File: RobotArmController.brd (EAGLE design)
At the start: 83.6 x 34.8 mm, 67 parts, among them M1 M02LOCK, M2 M02LOCK, M3 M02LOCK, M4 M02LOCK, M5 M02LOCK

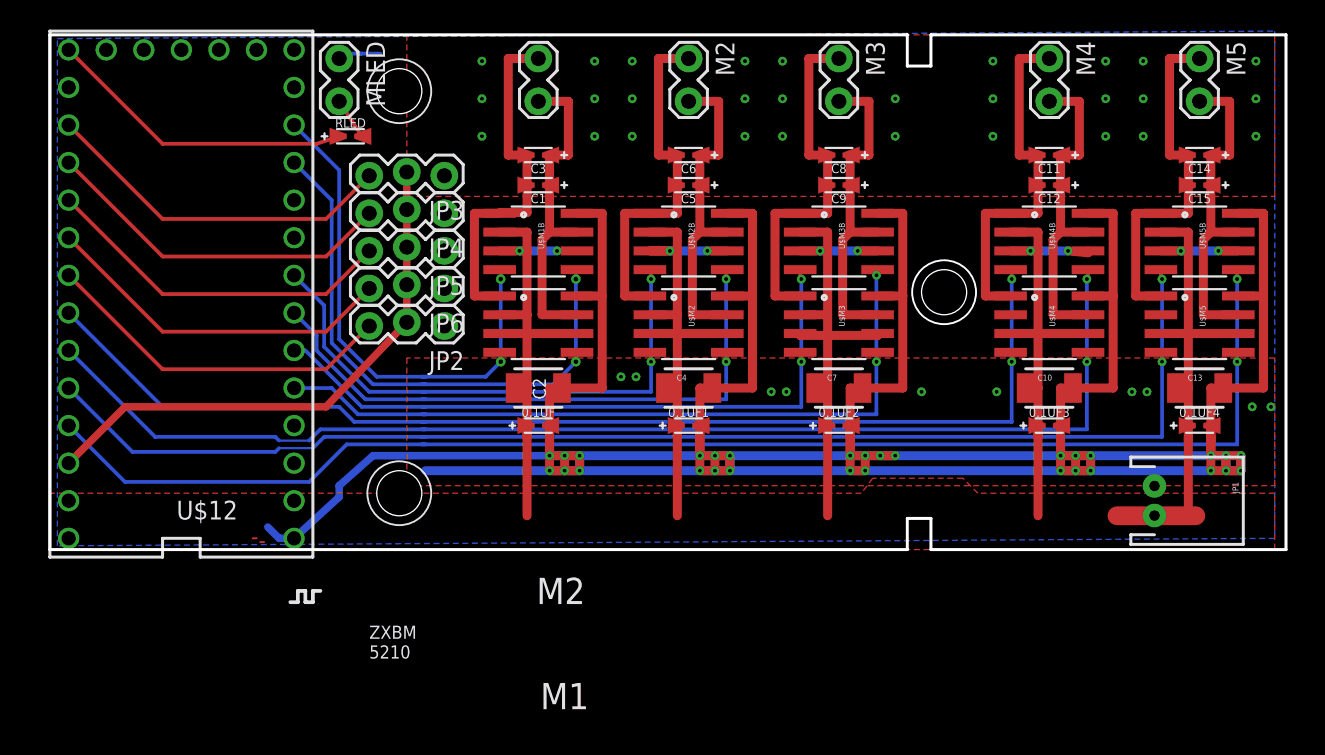
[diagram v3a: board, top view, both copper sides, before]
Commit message: Adjust for silkscreen and labels
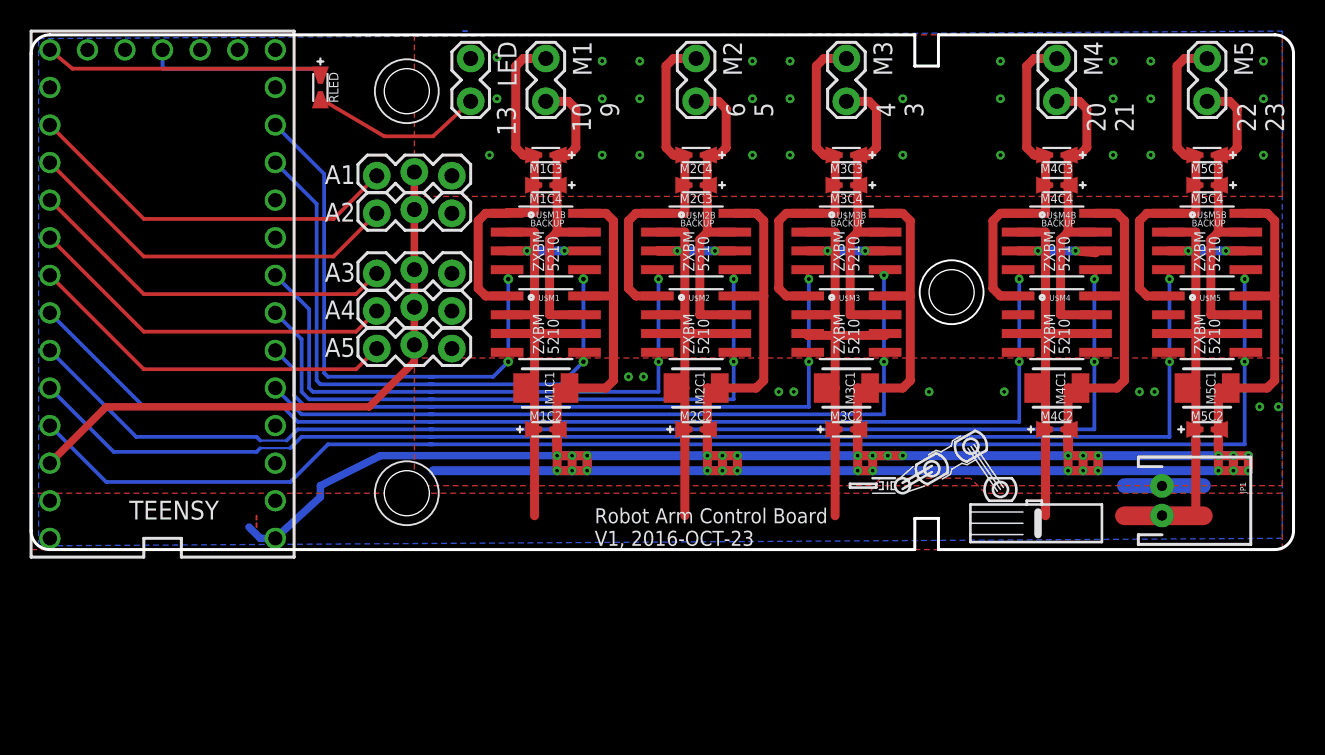
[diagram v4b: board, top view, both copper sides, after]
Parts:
- removed 0.1UF, 0.1UF1, 0.1UF2, 0.1UF3, 0.1UF4: (no value), tekdemo:0402-0603-0805-UNIVERSAL
- removed C1, C11, C12, C14, C15, C3, C5, C6, C8, C9: 0.1uf, tekdemo:0402-0603-0805-UNIVERSAL
- removed C10, C13, C2, C4, C7: (no value), tekdemo:1210
- removed JP2, JP3, JP4, JP5, JP6: (no value), tekdemo:1X03_LOCK
- removed MLED: M02LOCK, tekdemo:1X02_LOCK
- removed U$12: TEENSY_3.1_BASIC, Teensy_3_Series_Board_v1.0:TEENSY_3.1_BASIC
- added A1, A2, A3, A4, A5: (no value), tekdemo:1X03_LOCK
- added LED: M02LOCK, tekdemo:1X02_LOCK
- added M1C1, M2C1, M3C1, M4C1, M5C1: (no value), tekdemo:1210
- added M1C2, M2C2, M3C2, M4C2, M5C2: (no value), tekdemo:0402-0603-0805-UNIVERSAL
- added M1C3, M1C4, M2C3, M2C4, M3C3, M3C4, M4C3, M4C4, M5C3, M5C4: 0.1uf, tekdemo:0402-0603-0805-UNIVERSAL
- added TEENSY: TEENSY_3.1_BASIC, Teensy_3_Series_Board_v1.0:TEENSY_3.1_BASIC
- moved U$13 7.27 mm to (27.9, 45.2)
- moved RLED 3.88 mm to (18.3, 41.4), turned to 270 degrees
- moved U$4 1.55 mm to (14.0, 12.4), turned to 270 degrees
- moved U$24 1.37 mm to (14.0, 11.9), turned to 270 degrees
- moved U$9 0.57 mm to (68.8, 17.8)
- moved U$2 0.57 mm to (34.3, 17.8)
- moved U$3 0.57 mm to (42.9, 17.8)
- moved U$5 0.57 mm to (44.5, 17.8)
- moved U$7 0.57 mm to (54.6, 17.8)
- moved U$10 0.57 mm to (77.5, 17.5)
- moved U$11 0.57 mm to (79.0, 17.5)
- moved U$1 0.57 mm to (32.8, 17.8)
- moved U$6 0.57 mm to (53.1, 17.8)
- moved U$8 0.57 mm to (67.3, 17.8)
- moved M4 0.51 mm to (68.1, 43.2)
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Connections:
- removed net GND_LED: MLED.1, U$13.P$2
- net 3.3V: now also A1.2, A2.2, A3.2, A4.2, A5.2, TEENSY.3.3V, TEENSY.3.3V1; no longer JP2.2, JP3.2, JP4.2, JP5.2, JP6.2, U$12.3.3V, U$12.3.3V1
- net AGND: now also TEENSY.AGND; no longer U$12.AGND
- net GND: now also A1.1, A2.1, A3.1, A4.1, A5.1, LED.1, TEENSY.GND, TEENSY.GND1, U$13.P$2; no longer JP2.1, JP3.1, JP4.1, JP5.1, JP6.1, U$12.GND, U$12.GND1
- net GND_M1: now also M1C1.2, M1C2.-; no longer 0.1UF.-, C2.2
- net GND_M2: now also M2C1.2, M2C2.-; no longer 0.1UF1.-, C4.2
- net GND_M3: now also M3C1.2, M3C2.-; no longer 0.1UF2.-, C7.2
- net GND_M4: now also M4C1.2, M4C2.-; no longer 0.1UF3.-, C10.2
- net GND_M5: now also M5C1.2, M5C2.-; no longer 0.1UF4.-, C13.2
- net N$1: now also LED.2; no longer MLED.2
- net T10/PWM: now also TEENSY.10; no longer U$12.10
- net T13/LED: now also TEENSY.13; no longer U$12.13
- net T14/A0: now also TEENSY.14/A0; no longer U$12.14/A0
- net T15/A1: now also A1.3, TEENSY.15/A1; no longer JP3.3, U$12.15/A1
- net T16/A2: now also A2.3, TEENSY.16/A2; no longer JP4.3, U$12.16/A2
- net T17/A3: now also A3.3, TEENSY.17/A3; no longer JP5.3, U$12.17/A3
- net T18/A4: now also A4.3, TEENSY.18/A4; no longer JP6.3, U$12.18/A4
- net T19/A5: now also A5.3, TEENSY.19/A5; no longer JP2.3, U$12.19/A5
- net T20/PWM: now also TEENSY.20/A6; no longer U$12.20/A6
- net T21/PWM: now also TEENSY.21/A7; no longer U$12.21/A7
- net T22/PWM: now also TEENSY.22/A8; no longer U$12.22/A8
- net T23/PWM: now also TEENSY.23/A9; no longer U$12.23/A9
- net T3/PWM: now also TEENSY.3; no longer U$12.3
- net T4/PWM: now also TEENSY.4; no longer U$12.4
- net T5/PWM: now also TEENSY.5; no longer U$12.5
- net T6/PWM: now also TEENSY.6; no longer U$12.6
- net T9/PWM: now also TEENSY.9; no longer U$12.9
- net VBAT: now also TEENSY.VBAT; no longer U$12.VBAT
- net VIN: now also TEENSY.VIN; no longer U$12.VIN
- net VIN_M1: now also M1C1.1, M1C2.+; no longer 0.1UF.+, C2.1
- net VIN_M2: now also M2C1.1, M2C2.+; no longer 0.1UF1.+, C4.1
- net VIN_M3: now also M3C1.1, M3C2.+; no longer 0.1UF2.+, C7.1
- net VIN_M4: now also M4C1.1, M4C2.+; no longer 0.1UF3.+, C10.1
- net VIN_M5: now also M5C1.1, M5C2.+; no longer 0.1UF4.+, C13.1
- net VM1A: now also M1C3.-, M1C4.-; no longer C1.-, C3.-
- net VM1B: now also M1C3.+, M1C4.+; no longer C1.+, C3.+
- net VM2A: now also M2C3.-, M2C4.-; no longer C5.-, C6.-
- net VM2B: now also M2C3.+, M2C4.+; no longer C5.+, C6.+
- net VM3A: now also M3C3.-, M3C4.-; no longer C8.-, C9.-
- net VM3B: now also M3C3.+, M3C4.+; no longer C8.+, C9.+
- net VM4A: now also M4C3.-, M4C4.-; no longer C11.-, C12.-
- net VM4B: now also M4C3.+, M4C4.+; no longer C11.+, C12.+
- net VM5A: now also M5C3.-, M5C4.-; no longer C14.-, C15.-
- net VM5B: now also M5C3.+, M5C4.+; no longer C14.+, C15.+
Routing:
- net GND: track 181.2 -> 196.3 mm
- net N$1: track 2.81 -> 11.8 mm
- net T6/PWM: track 13.8 -> 17.1 mm
- net T5/PWM: track 11.9 -> 15.2 mm
- net 3.3V: track 37.0 -> 40.3 mm
- net T9/PWM: track 20.8 -> 23.9 mm
- net T10/PWM: track 22.6 -> 25.6 mm
- net T4/PWM: track 10.5 -> 13.3 mm
- net T20/PWM: track 27.2 -> 29.0 mm
- net T3/PWM: track 9.63 -> 11.4 mm
- net T23/PWM: track 26.8 -> 28.5 mm
- net T22/PWM: track 26.3 -> 28.1 mm
- net T21/PWM: track 27.0 -> 28.7 mm
- net T16/A2: track 24.2 -> 25.9 mm
- net T15/A1: track 24.2 -> 25.9 mm
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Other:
- board size 83.6 x 34.8 mm -> 85.3 x 34.8 mm
- board text added: "10 9"
- board text added: "13"
- board text added: "20 21"
- board text added: "22 23"
- board text added: "4 3"
- board text added: "6 5"
- board text added: "BACKUP"
- board text added: "Robot Arm Control Board V1, 2016-OCT-23"
- board text removed: "+"
- board text removed: "3-18V,1.5A"
- board text removed: "3NOV2015"
- board text removed: "A"
- board text removed: "GND"
- board text removed: "M1"
- board text removed: "M2"
- board text removed: "ZXBM5201 MOTOR BOARD"
